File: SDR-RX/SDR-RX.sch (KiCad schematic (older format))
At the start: 15 parts, among them U1 Si4734-D60-GU, Y1 32.768MHz

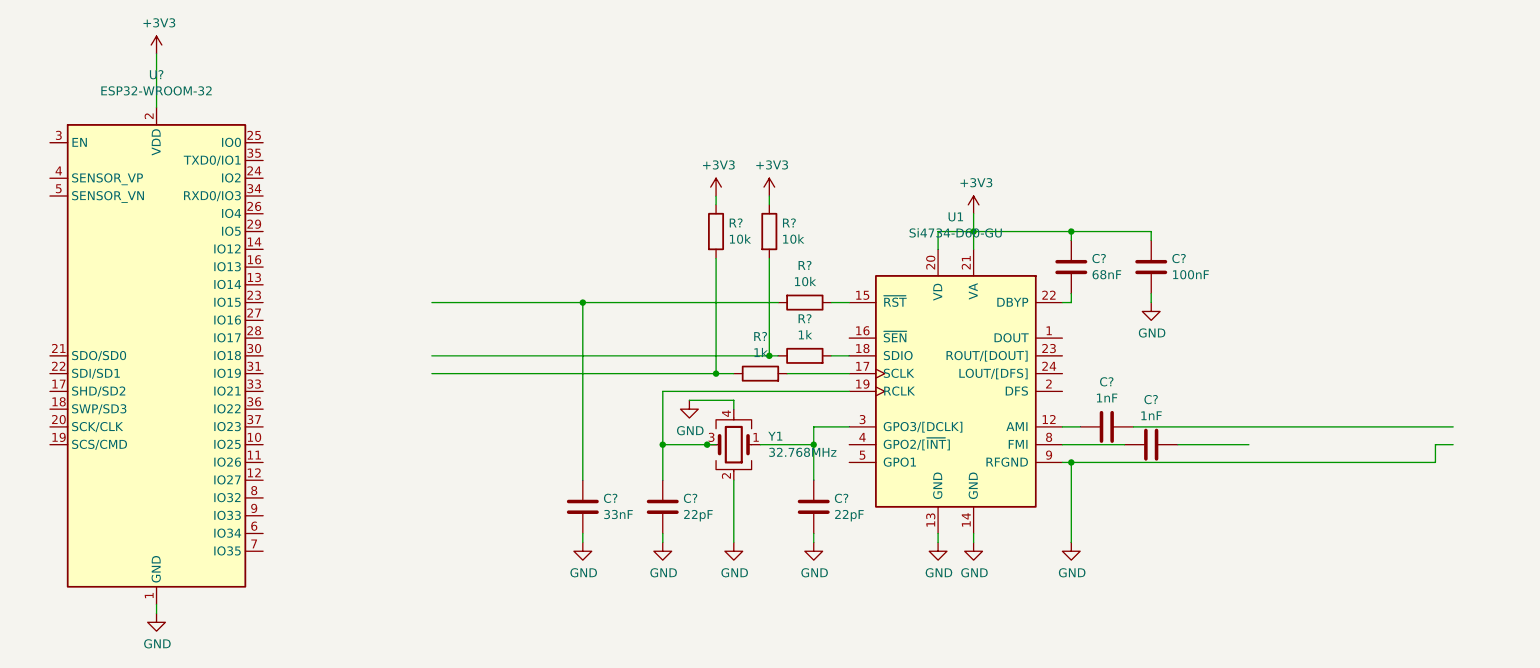
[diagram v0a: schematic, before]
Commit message: Added pullups/down to GPO1, GPO2 of RF and EN of ESP
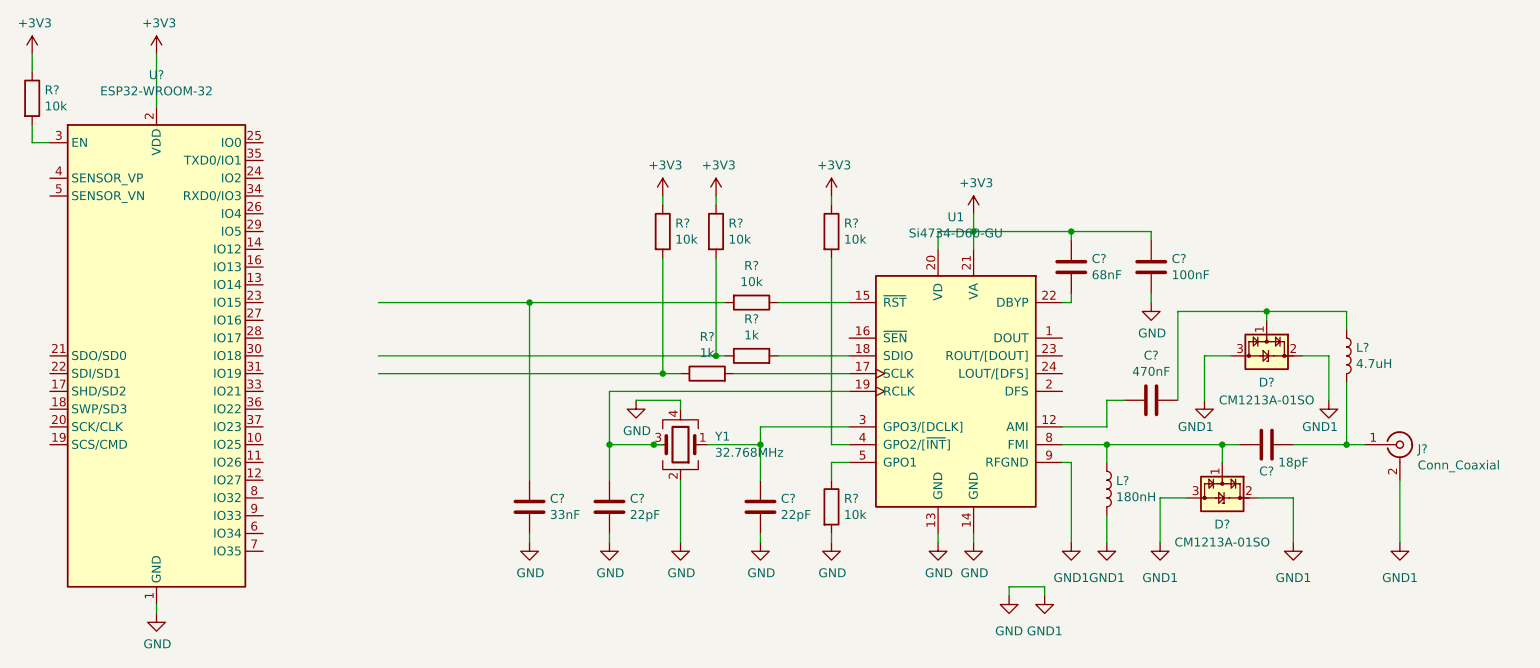
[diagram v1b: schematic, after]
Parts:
- removed C?: 1nF, Capacitor_SMD:C_0603_1608Metric_Pad1.08x0.95mm_HandSolder, symbol Device:C
- added C?: 470nF, Capacitor_SMD:C_0603_1608Metric_Pad1.08x0.95mm_HandSolder, symbol Device:C
- added D? (x2): CM1213A-01SO, Package_TO_SOT_SMD:SOT-23, symbol Power_Protection:CM1213A-01SO
- added J?: Conn_Coaxial, Connector_Coaxial:SMA_Samtec_SMA-J-P-X-ST-EM1_EdgeMount, symbol Connector:Conn_Coaxial
- added L?: 180nH, Inductor_SMD:L_0603_1608Metric_Pad1.05x0.95mm_HandSolder, symbol Device:L
- added L?: 4.7uH, Inductor_SMD:L_0603_1608Metric_Pad1.05x0.95mm_HandSolder, symbol Device:L
- added R? (x3): 10k, Resistor_SMD:R_0603_1608Metric_Pad0.98x0.95mm_HandSolder, symbol Device:R
- added RFGND, RFGND? (x7): GND1, symbol power:GND1
- C?: value 1nF -> 18pF; LCSC Part # C1588 -> C1647
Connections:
- wire segments 53 -> 84
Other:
- moved on the sheet: C?, R?, Y1

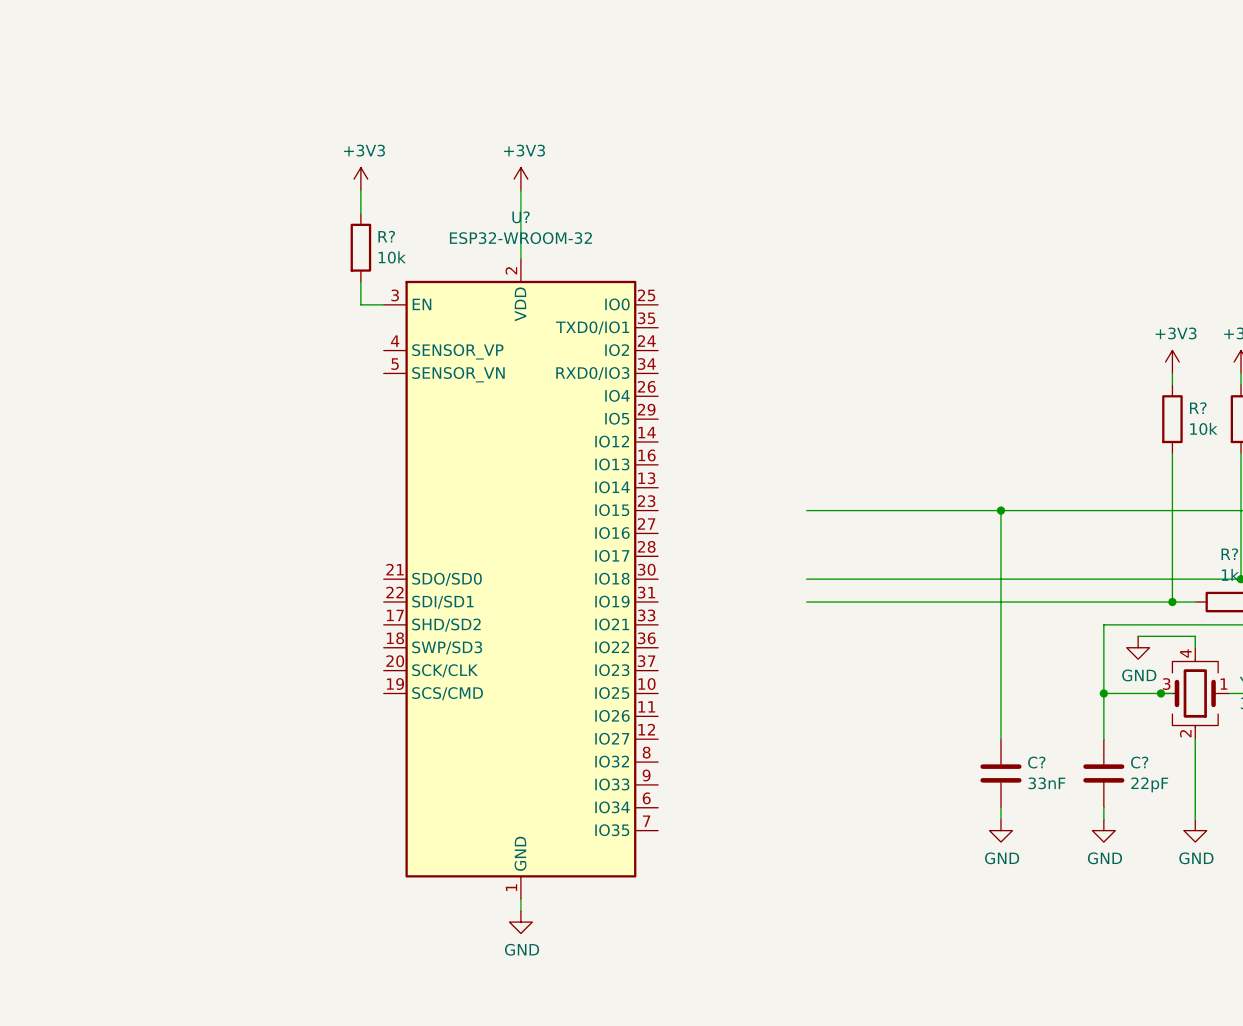
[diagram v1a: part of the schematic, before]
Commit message: Added Peripheral Schematics for ESP32-WROOM-32-D 3V3 regulator still missing
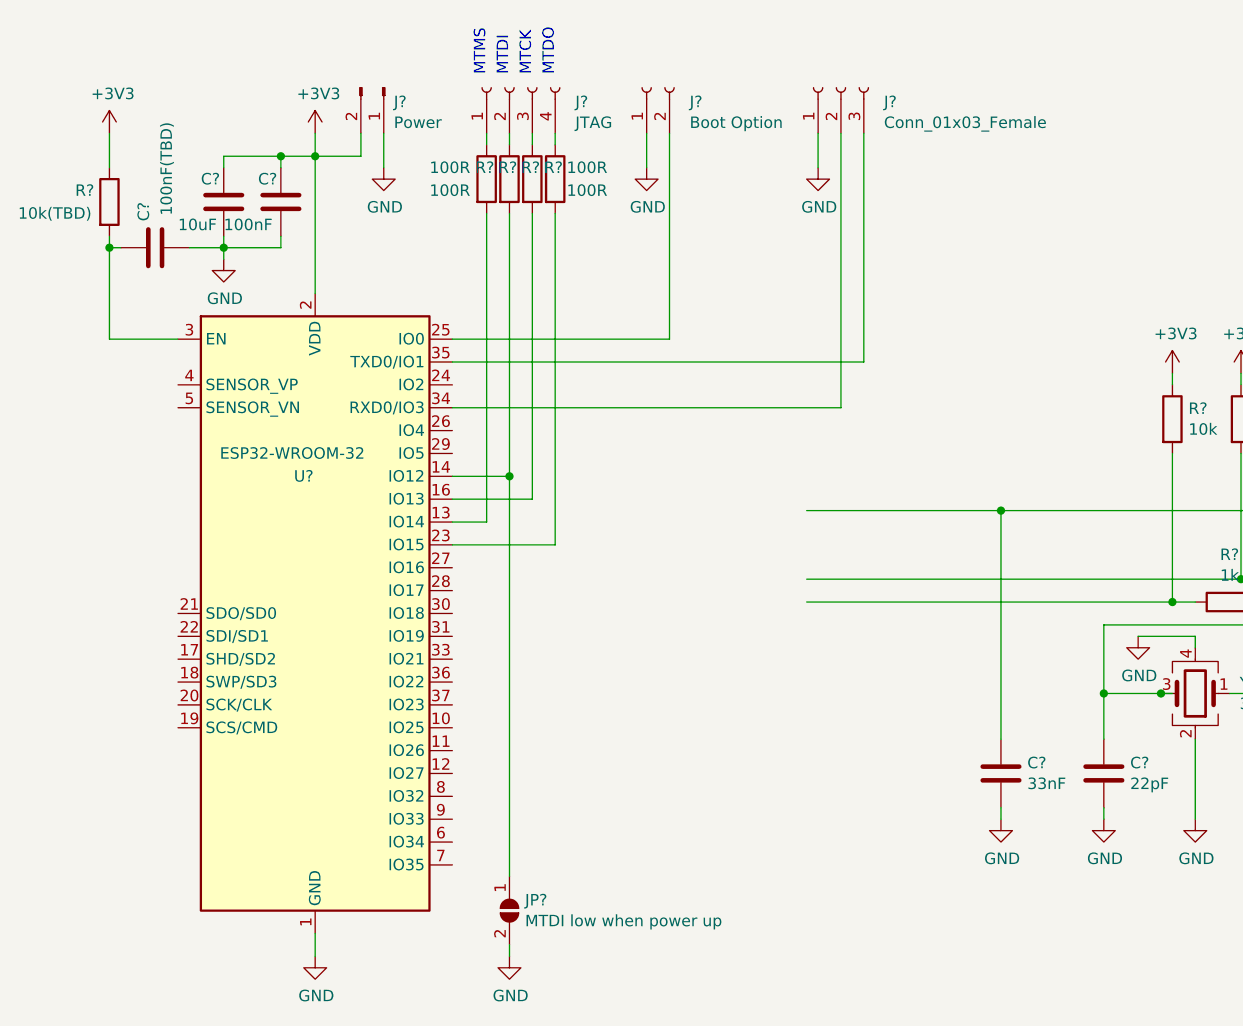
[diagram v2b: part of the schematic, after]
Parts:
- added C?: 100nF, Capacitor_SMD:C_0603_1608Metric_Pad1.08x0.95mm_HandSolder, symbol Device:C
- added C?: 10uF, Capacitor_SMD:C_0603_1608Metric_Pad1.08x0.95mm_HandSolder, symbol Device:C
- added C?: 100nF(TBD), Capacitor_SMD:C_0603_1608Metric_Pad1.08x0.95mm_HandSolder, symbol Device:C
- added J?: JTAG, symbol Connector:Conn_01x04_Female
- added J?: Boot Option, symbol Connector:Conn_01x02_Female
- added J?: Conn_01x03_Female, symbol Connector:Conn_01x03_Female
- added J?: Power, symbol Connector:Conn_01x02_Male
- added JP?: MTDI low when power up, symbol Jumper:SolderJumper_2_Open
- added R? (x4): 100R, Resistor_SMD:R_0603_1608Metric_Pad0.98x0.95mm_HandSolder, symbol Device:R
- R?: value 10k -> 10k(TBD)
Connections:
- wire segments 84 -> 121
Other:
- note added: "MTCK"
- note added: "MTDI"
- note added: "MTDO"
- note added: "MTMS"
- moved on the sheet: R?, U?

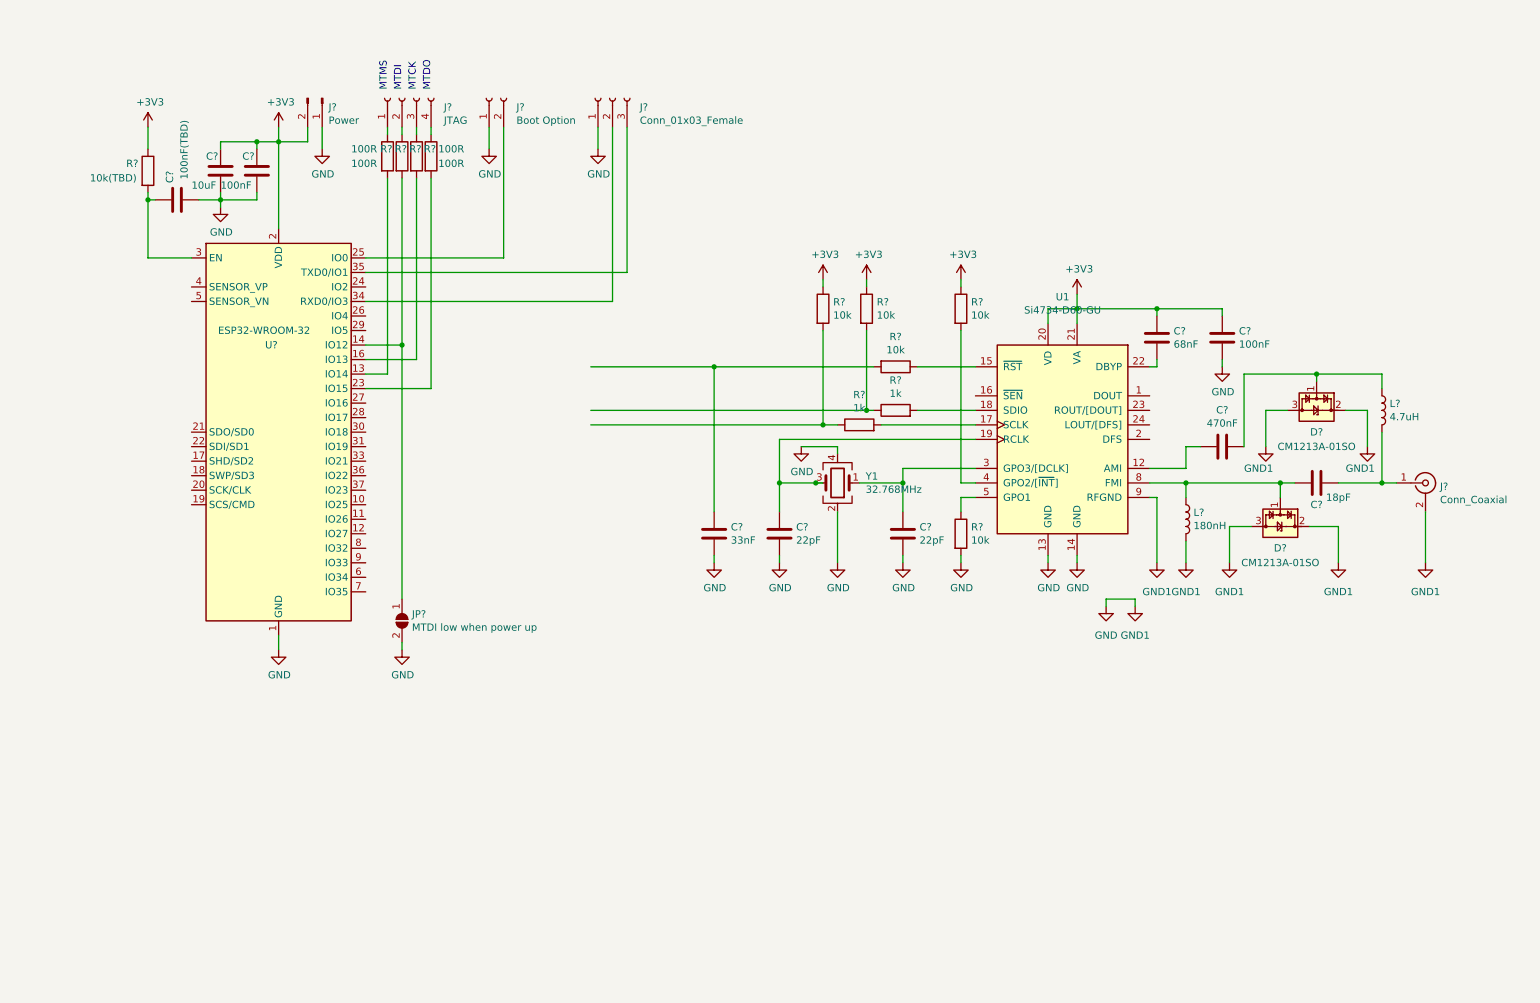
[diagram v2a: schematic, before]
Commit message: Added power supply path
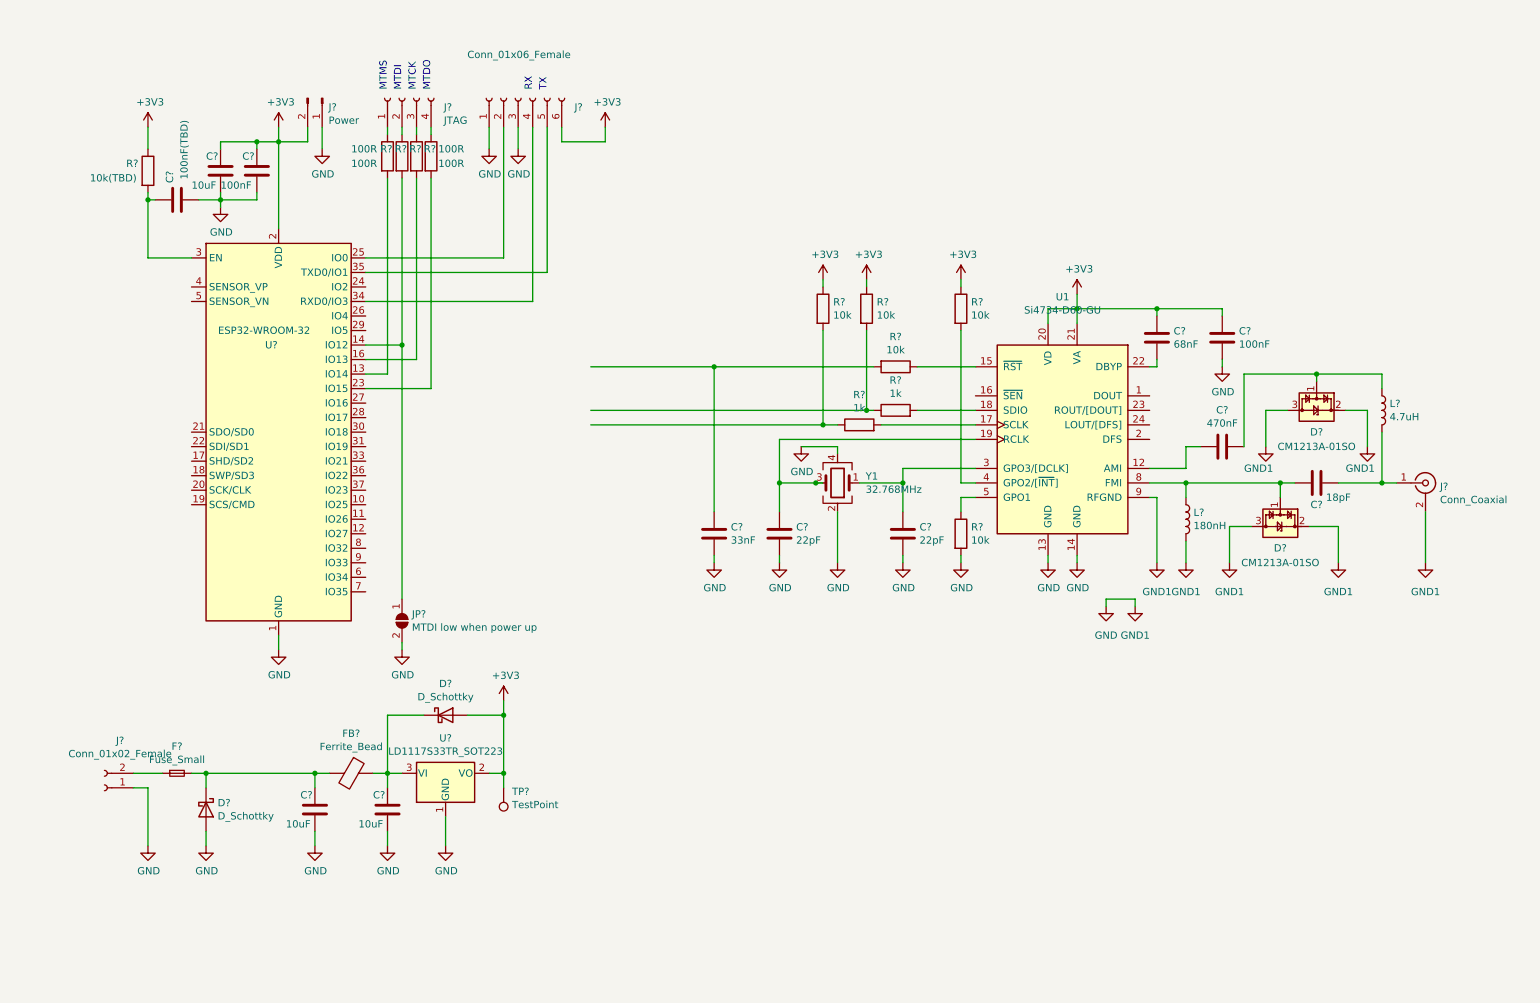
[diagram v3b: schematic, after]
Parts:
- removed J?: Boot Option, symbol Connector:Conn_01x02_Female
- removed J?: Conn_01x03_Female, symbol Connector:Conn_01x03_Female
- added C? (x2): 10uF, Capacitor_SMD:C_0805_2012Metric_Pad1.18x1.45mm_HandSolder, symbol Device:C
- added D? (x2): D_Schottky, symbol Device:D_Schottky
- added F?: Fuse_Small, symbol Device:Fuse_Small
- added FB?: Ferrite_Bead, symbol Device:Ferrite_Bead
- added J?: Conn_01x06_Female, symbol Connector:Conn_01x06_Female
- added J?: Conn_01x02_Female, symbol Connector:Conn_01x02_Female
- added TP?: TestPoint, symbol Connector:TestPoint
- added U?: LD1117S33TR_SOT223, Package_TO_SOT_SMD:SOT-223-3_TabPin2, symbol Regulator_Linear:LD1117S33TR_SOT223
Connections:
- wire segments 121 -> 146
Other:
- note added: "RX"
- note added: "TX"

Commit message: Changes at ESP Reset, Data/Clock wired, Antenna changes
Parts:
- removed C?: 10uF, Capacitor_SMD:C_0603_1608Metric_Pad1.08x0.95mm_HandSolder, symbol Device:C
- removed C?: 100nF(TBD), Capacitor_SMD:C_0603_1608Metric_Pad1.08x0.95mm_HandSolder, symbol Device:C
- removed C?: 10uF, Capacitor_SMD:C_0805_2012Metric_Pad1.18x1.45mm_HandSolder, symbol Device:C
- removed D? (x2): D_Schottky, symbol Device:D_Schottky
- removed J?: JTAG, symbol Connector:Conn_01x04_Female
- removed J?: Power, symbol Connector:Conn_01x02_Male
- removed JP?: MTDI low when power up, symbol Jumper:SolderJumper_2_Open
- removed L?: 4.7uH, Inductor_SMD:L_0603_1608Metric_Pad1.05x0.95mm_HandSolder, symbol Device:L
- removed R? (x2): 1k, Resistor_SMD:R_0603_1608Metric_Pad0.98x0.95mm_HandSolder, symbol Device:R
- removed R? (x2): 10k, Resistor_SMD:R_0603_1608Metric_Pad0.98x0.95mm_HandSolder, symbol Device:R
- removed R? (x4): 100R, Resistor_SMD:R_0603_1608Metric_Pad0.98x0.95mm_HandSolder, symbol Device:R
- added C? (x3): 10uF, Capacitor_SMD:C_1206_3216Metric_Pad1.33x1.80mm_HandSolder, symbol Device:C
- added C?: 100nF, Capacitor_SMD:C_0603_1608Metric_Pad1.08x0.95mm_HandSolder, symbol Device:C
- added D? (x2): SM4007, Diode_SMD:D_MELF, symbol Diode:SM4007
- added J?: Conn_01x03_Male, symbol Connector:Conn_01x03_Male
- added J?: Conn_Coaxial, Connector_Coaxial:SMA_Samtec_SMA-J-P-X-ST-EM1_EdgeMount, symbol Connector:Conn_Coaxial
- added Q? (x2): S8050, Package_TO_SOT_SMD:SOT-23_Handsoldering, symbol Transistor_BJT:S8050
- added R? (x2): 12k, Resistor_SMD:R_0603_1608Metric_Pad0.98x0.95mm_HandSolder, symbol Device:R
- added RFGND?: GND1, symbol power:GND1
- added SW?: Reset ESP, Button_Switch_SMD:SW_SPST_B3SL-1002P, symbol Switch:SW_MEC_5E
- added TP?: Reset SI4734, symbol Connector:TestPoint
- added TP?: Data, symbol Connector:TestPoint
- added TP?: Clock, symbol Connector:TestPoint
- added TP?: Reset ESP, symbol Connector:TestPoint
- C?: footprint Capacitor_SMD:C_0805_2012Metric_Pad1.18x1.45mm_HandSolder -> Capacitor_SMD:C_1206_3216Metric_Pad1.33x1.80mm_HandSolder; LCSC Part # C46653 -> C13585
- F?: value Fuse_Small -> Fuse_1A; footprint (none) -> Fuse:Fuse_1206_3216Metric_Pad1.42x1.75mm_HandSolder; LCSC Part # (none) -> C182308
- FB?: value Ferrite_Bead -> 0Ω @ 100MHZ 1A; footprint (none) -> Inductor_SMD:L_1206_3216Metric_Pad1.22x1.90mm_HandSolder; LCSC Part # (none) -> C94305
- J?: value Conn_01x06_Female -> Program; footprint (none) -> Connector_JST:JST_XH_S7B-XH-A-1_1x07_P2.50mm_Horizontal; symbol Connector:Conn_01x06_Female -> Connector:Conn_01x07_Female
- L?: value 180nH -> 470nH; LCSC Part # C21430 -> C1034
- R?: value 10k(TBD) -> 10k
- Y1: value 32.768MHz -> 32.768kHz; footprint (none) -> Crystal:Crystal_SMD_3215-2Pin_3.2x1.5mm; symbol Device:Crystal_GND24 -> Device:Crystal; LCSC Part # C9009 -> C32346
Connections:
- net +3V3: now also J?.5 (Pin_5), C?.1, C?.1, C?.1, D?.2 (A); no longer J?.6 (Pin_6)
- net GND: now also C?.2, C?.2, C?.2, C?.2, D?.2 (A), J?.1 (Pin_1), J?.2 (Ext), J?.2 (Pin_2), J?.3 (Pin_3), RFGND?.1 (GND1), SW?.1, SW?.2; no longer J?.3 (Pin_3), Y1.2, Y1.4
- net at R?.1, U1.15 (~RST): now also C?.1, TP?.1
- net at U1.16 (~SEN): now also R?.2
- net at U1.17 (SCLK): now also R?.2, U?.22 (SDI/SD1), TP?.1
- net at U1.18 (SDIO): now also R?.2, U?.21 (SDO/SD0), TP?.1
- net at C?.2, U1.19 (RCLK): now also Y1.2; no longer Y1.3
- net at U?.14 (IO12): now also R?.2
- net at U?.25 (IO0): now also Q?.3 (C); no longer J?.2 (Pin_2)
- net at U?.3 (EN): now also Q?.3 (C), SW?.3 (K), SW?.4 (A), TP?.1; no longer R?.2
- net at U?.34 (RXD0/IO3): now also J?.3 (Pin_3); no longer J?.4 (Pin_4)
- net at U?.35 (TXD0/IO1): now also J?.2 (Pin_2); no longer J?.5 (Pin_5)
- net at C?.1, D?.1 (CH1): now also J?.1 (In)
- net at F?.2, FB?.2: now also C?.1, D?.1 (K)
- net at C?.1, FB?.1, U?.3 (VI): now also D?.1 (K)
- new net: J?.6 (Pin_6), Q?.1 (E), R?.1
- new net: J?.7 (Pin_7), Q?.1 (E), R?.1
- new net: Q?.2 (B), R?.2 (x2)
- no-connect marks 0 -> 3
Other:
- note added: "3V3"
- note added: "5V"
- note added: "DTR"
- note added: "GND"
- note added: "RTS"
- note removed: "MTCK"
- note removed: "MTDI"
- note removed: "MTDO"
- note removed: "MTMS"
- moved on the sheet: C?, D?, F?, FB?, J?, L?, R?, TP?, U1, U?
